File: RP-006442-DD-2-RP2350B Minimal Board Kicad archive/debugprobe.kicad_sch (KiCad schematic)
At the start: 42 parts, among them J4 Conn_01x03, J5 USB_C_Receptacle_USB2.0_16P, SW3 SW_Push, SW4 SW_Push, U5 W25Q128JVS, U6 NCP1117-3.3_SOT223, U7 RP2350_60QFN, Y2 ABM8-272-T3

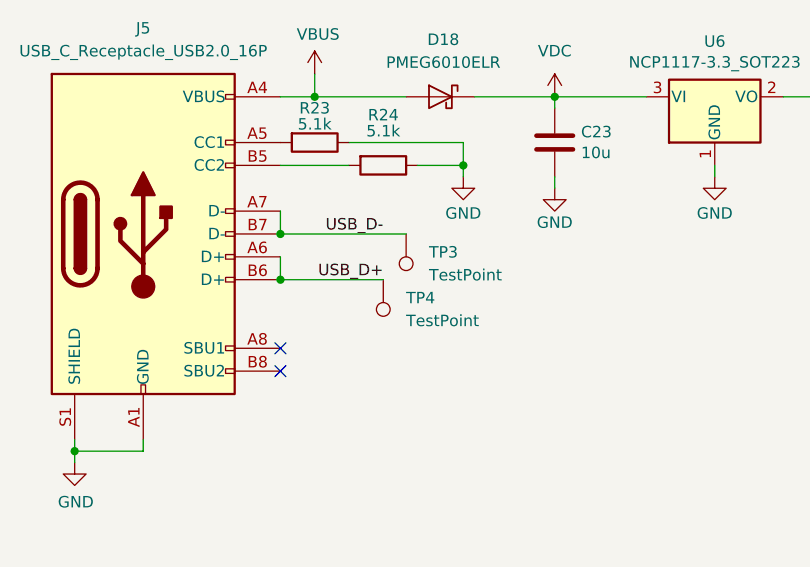
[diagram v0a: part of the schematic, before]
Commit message: Update to schematic and pcb
Changed:
- Added 100n decoupling capacitors to both 74HC595
- Changed ground plane to single common ground plane
- Added schottky diode to usb vbus inputs, creating separate vbus and vsys
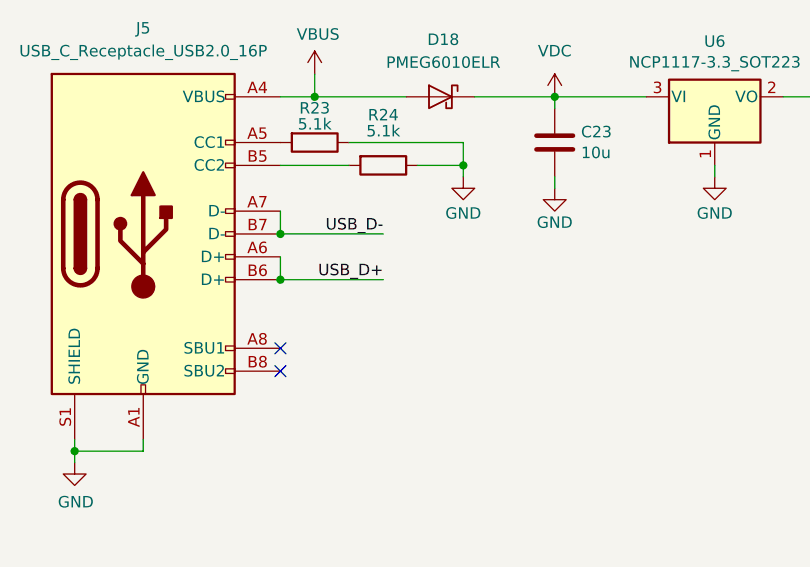
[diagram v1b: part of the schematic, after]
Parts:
- removed TP3, TP4: TestPoint, TestPoint:TestPoint_Pad_2.0x2.0mm, symbol Connector:TestPoint
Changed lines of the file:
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@@
 	)
 	(junction
+		(at 52.07 55.88)
+		(diameter 0)
+		(color 0 0 0 0)
+	)
+	(junction
 		(at 241.3 63.5)
 		(diameter 0)
@@
 	)
 	(junction
-		(at 52.07 55.88)
-		(diameter 0)
-		(color 0 0 0 0)
-	)
-	(junction
 		(at 161.29 73.66)
 		(diameter 0)
@@
 	(wire
 		(pts
-			(xy 298.45 64.77) (xy 298.45 63.5)
+			(xy 52.07 55.88) (xy 63.5 55.88)
 		)
 		(stroke
@@
 	(wire
 		(pts
-			(xy 125.73 118.11) (xy 172.72 118.11)
+			(xy 298.45 64.77) (xy 298.45 63.5)
 		)
 		(stroke
@@
 	(wire
 		(pts
-			(xy 220.98 63.5) (xy 220.98 83.82)
+			(xy 125.73 118.11) (xy 172.72 118.11)
 		)
 		(stroke
@@
 	(wire
 		(pts
-			(xy 252.73 74.93) (xy 241.3 74.93)
+			(xy 220.98 63.5) (xy 220.98 83.82)
 		)
 		(stroke
@@
 	(wire
 		(pts
-			(xy 294.64 189.23) (xy 309.88 189.23)
+			(xy 252.73 74.93) (xy 241.3 74.93)
 		)
 		(stroke
@@
 	(wire
 		(pts
-			(xy 66.04 55.88) (xy 52.07 55.88)
+			(xy 294.64 189.23) (xy 309.88 189.23)
 		)
 		(stroke
@@
 	)
 	(symbol
-		(lib_id "Connector:TestPoint")
-		(at 63.5 60.96 180)
-		(unit 1)
-		(exclude_from_sim no)
-		(in_bom yes)
-		(on_board yes)
-		(dnp no)
-		(fields_autoplaced yes)
-		(property "Reference" "TP4"
-			(at 66.04 62.9919 0)
-			(effects
-				(font
-					(size 1.27 1.27)
-				)
-				(justify right)
-			)
-		)
-		(property "Value" "TestPoint"
-			(at 66.04 65.5319 0)
-			(effects
-				(font
-					(size 1.27 1.27)
-				)
-				(justify right)
-			)
-		)
-		(property "Footprint" "TestPoint:TestPoint_Pad_2.0x2.0mm"
-			(at 58.42 60.96 0)
-			(effects
-				(font
-					(size 1.27 1.27)
-				)
-				(hide yes)
-			)
-		)
-		(property "Datasheet" "~"
-			(at 58.42 60.96 0)
-			(effects
-				(font
-					(size 1.27 1.27)
-				)
-				(hide yes)
-			)
-		)
-		(property "Description" "test point"
-			(at 63.5 60.96 0)
-			(effects
-				(font
-					(size 1.27 1.27)
-				)
-				(hide yes)
-			)
-		)
-		(pin "1"
-		)
-		(instances
-			(project "RP2350_80QFN_minimal"
-				(path "/94683f5c-9cd9-448e-be96-9792537b5cb8/500e1af8-c8c5-44c6-9fbe-f4d5e5ab4ca8"
-					(reference "TP4")
-					(unit 1)
-				)
-			)
-		)
-	)
-	(symbol
 		(lib_id "power:GND")
 		(at 298.45 76.835 0)
@@
 					(unit 1)
 				)
-			)
-		)
-	)
-	(symbol
-		(lib_id "Connector:TestPoint")
-		(at 66.04 55.88 180)
-		(unit 1)
-		(exclude_from_sim no)
-		(in_bom yes)
-		(on_board yes)
-		(dnp no)
-		(fields_autoplaced yes)
-		(property "Reference" "TP3"
-			(at 68.58 57.9119 0)
-			(effects
-				(font
-					(size 1.27 1.27)
-				)
-				(justify right)
-			)
-		)
-		(property "Value" "TestPoint"
-			(at 68.58 60.4519 0)
-			(effects
-				(font
-					(size 1.27 1.27)
-				)
-				(justify right)
-			)
-		)
-		(property "Footprint" "TestPoint:TestPoint_Pad_2.0x2.0mm"
-			(at 60.96 55.88 0)
-			(effects
-				(font
-					(size 1.27 1.27)
-				)
-				(hide yes)
-			)
-		)
-		(property "Datasheet" "~"
-			(at 60.96 55.88 0)
-			(effects
-				(font
-					(size 1.27 1.27)
-				)
-				(hide yes)
-			)
-		)
-		(property "Description" "test point"
-			(at 66.04 55.88 0)
-			(effects
-				(font
-					(size 1.27 1.27)
-				)
-				(hide yes)
-			)
-		)
-		(pin "1"
-		)
-		(instances
-			(project "RP2350_80QFN_minimal"
-				(path "/94683f5c-9cd9-448e-be96-9792537b5cb8/500e1af8-c8c5-44c6-9fbe-f4d5e5ab4ca8"
-					(reference "TP3")
-					(unit 1)
-				)

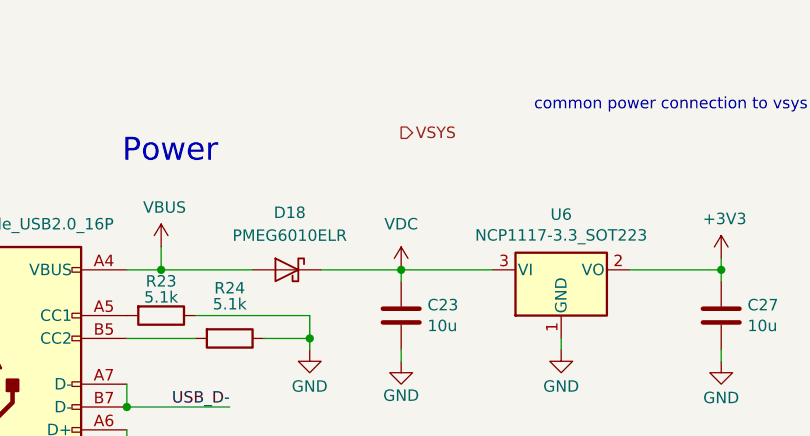
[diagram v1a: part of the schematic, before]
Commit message: Update PCB
Created footprint for SW_SPDT symbol

Added switch footprint to PCB and connected VSYS
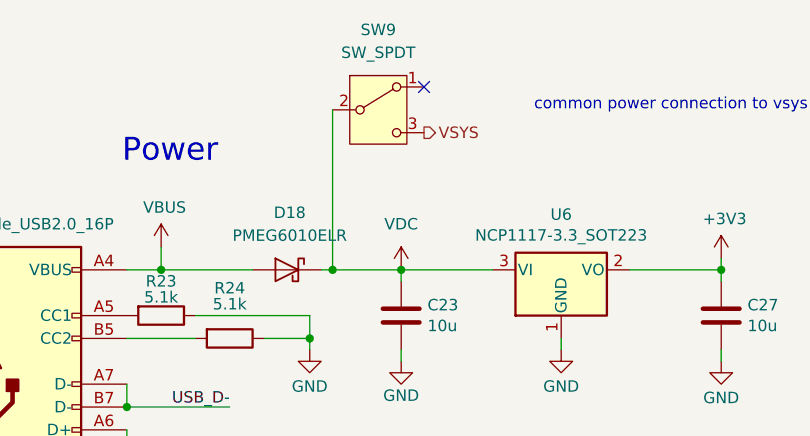
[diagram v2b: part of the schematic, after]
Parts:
- added SW9: SW_SPDT, Button_Switch_SMD:SW_SPDT_HRO_K3-1235S-K1, symbol Switch:SW_SPDT
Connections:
- net VDC: now also SW9.2 (B)
- net VSYS: now also SW9.3 (C)
- no-connect marks 2 -> 3
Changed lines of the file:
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@@
 	)
 	(junction
+		(at 74.93 40.64)
+		(diameter 0)
+		(color 0 0 0 0)
+	)
+	(junction
 		(at 213.36 83.82)
 		(diameter 0)
@@
 	)
 	(no_connect
+		(at 85.09 20.32)
+	)
+	(no_connect
 		(at 52.07 68.58)
 	)
@@
 	(wire
 		(pts
-			(xy 73.66 40.64) (xy 82.55 40.64)
+			(xy 73.66 40.64) (xy 74.93 40.64)
 		)
 		(stroke
@@
 	(wire
 		(pts
+			(xy 74.93 40.64) (xy 82.55 40.64)
+		)
+		(stroke
+			(width 0)
+			(type default)
+		)
+	)
+	(wire
+		(pts
 			(xy 275.59 64.77) (xy 275.59 63.5)
 		)
@@
 	(wire
 		(pts
+			(xy 74.93 22.86) (xy 74.93 40.64)
+		)
+		(stroke
+			(width 0)
+			(type default)
+		)
+	)
+	(wire
+		(pts
 			(xy 90.17 246.38) (xy 91.44 246.38)
 		)
@@
 	(hierarchical_label "VSYS"
 		(shape output)
-		(at 82.55 25.4 0)
+		(at 85.09 25.4 0)
 		(effects
 			(font
@@
 					(unit 1)
 				)
+			)
+		)
+	)
+	(symbol
+		(lib_id "Switch:SW_SPDT")
+		(at 80.01 22.86 0)
+		(unit 1)
+		(exclude_from_sim no)
+		(in_bom yes)
+		(on_board yes)
+		(dnp no)
+		(fields_autoplaced yes)
+		(property "Reference" "SW9"
+			(at 80.01 13.97 0)
+			(effects
+				(font
+					(size 1.27 1.27)
+				)
+			)
+		)
+		(property "Value" "SW_SPDT"
+			(at 80.01 16.51 0)
+			(effects
+				(font
+					(size 1.27 1.27)
+				)
+			)
+		)
+		(property "Footprint" "Button_Switch_SMD:SW_SPDT_HRO_K3-1235S-K1"
+			(at 80.01 22.86 0)
+			(effects
+				(font
+					(size 1.27 1.27)
+				)
+				(hide yes)
+			)
+		)
+		(property "Datasheet" "~"
+			(at 80.01 30.48 0)
+			(effects
+				(font
+					(size 1.27 1.27)
+				)
+				(hide yes)
+			)
+		)
+		(property "Description" "Switch, single pole double throw"
+			(at 80.01 22.86 0)
+			(effects
+				(font
+					(size 1.27 1.27)
+				)
+				(hide yes)
+			)
+		)
+		(pin "1"
+		)
+		(pin "3"
+		)
+		(pin "2"
+		)
+		(instances
+			(project ""
+				(path "/94683f5c-9cd9-448e-be96-9792537b5cb8/500e1af8-c8c5-44c6-9fbe-f4d5e5ab4ca8"
+					(reference "SW9")
+					(unit 1)
+				)

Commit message: Update debugprobe.kicad_sch
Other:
- note removed: "IOs"
- moved on the sheet: C23, C27, C28, C29, C30, C31, C32, C33, C34, C35, C36, C37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

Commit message: Big update
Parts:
- removed D18: PMEG6010ELR, Diode_SMD:Nexperia_CFP3_SOD-123W, symbol Diode:PMEG6010ELR
- added D28: PMEG6010ELR, Diode_SMD:Nexperia_CFP3_SOD-123W, symbol Diode:PMEG6010ELR
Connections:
- net VBUS: now also D28.2 (A)
- net VDC: now also D28.1 (K)
- net GPIO10: no longer names the net of U7.14 (GPIO10)
- net GPIO11: no longer names the net of U7.15 (GPIO11)
- net GPIO12: no longer names the net of U7.16 (GPIO12)
- net GPIO13: no longer names the net of U7.17 (GPIO13)
- net GPIO14: no longer names the net of U7.18 (GPIO14)
- net GPIO15: no longer names the net of U7.19 (GPIO15)
- net GPIO16: no longer names the net of U7.27 (GPIO16)
- net GPIO17: no longer names the net of U7.28 (GPIO17)
- net GPIO18: no longer names the net of U7.29 (GPIO18)
- net GPIO19: no longer names the net of U7.31 (GPIO19)
- net GPIO20: no longer names the net of U7.32 (GPIO20)
- net GPIO21: no longer names the net of U7.33 (GPIO21)
- net GPIO22: no longer names the net of U7.34 (GPIO22)
- net GPIO23: no longer names the net of U7.35 (GPIO23)
- net GPIO24: no longer names the net of U7.36 (GPIO24)
- net GPIO25: no longer names the net of U7.37 (GPIO25)
- net GPIO26_ADC0: no longer names the net of U7.40 (GPIO26_ADC0)
- net GPIO27_ADC1: no longer names the net of U7.41 (GPIO27_ADC1)
- net GPIO28_ADC2: no longer names the net of U7.42 (GPIO28_ADC2)
- net GPIO29_ADC3: no longer names the net of U7.43 (GPIO29_ADC3)
- net GPIO6: no longer names the net of U7.9 (GPIO6)
- net GPIO7: no longer names the net of U7.10 (GPIO7)
- net GPIO8: no longer names the net of U7.12 (GPIO8)
- net GPIO9: no longer names the net of U7.13 (GPIO9)
- no-connect marks 3 -> 28

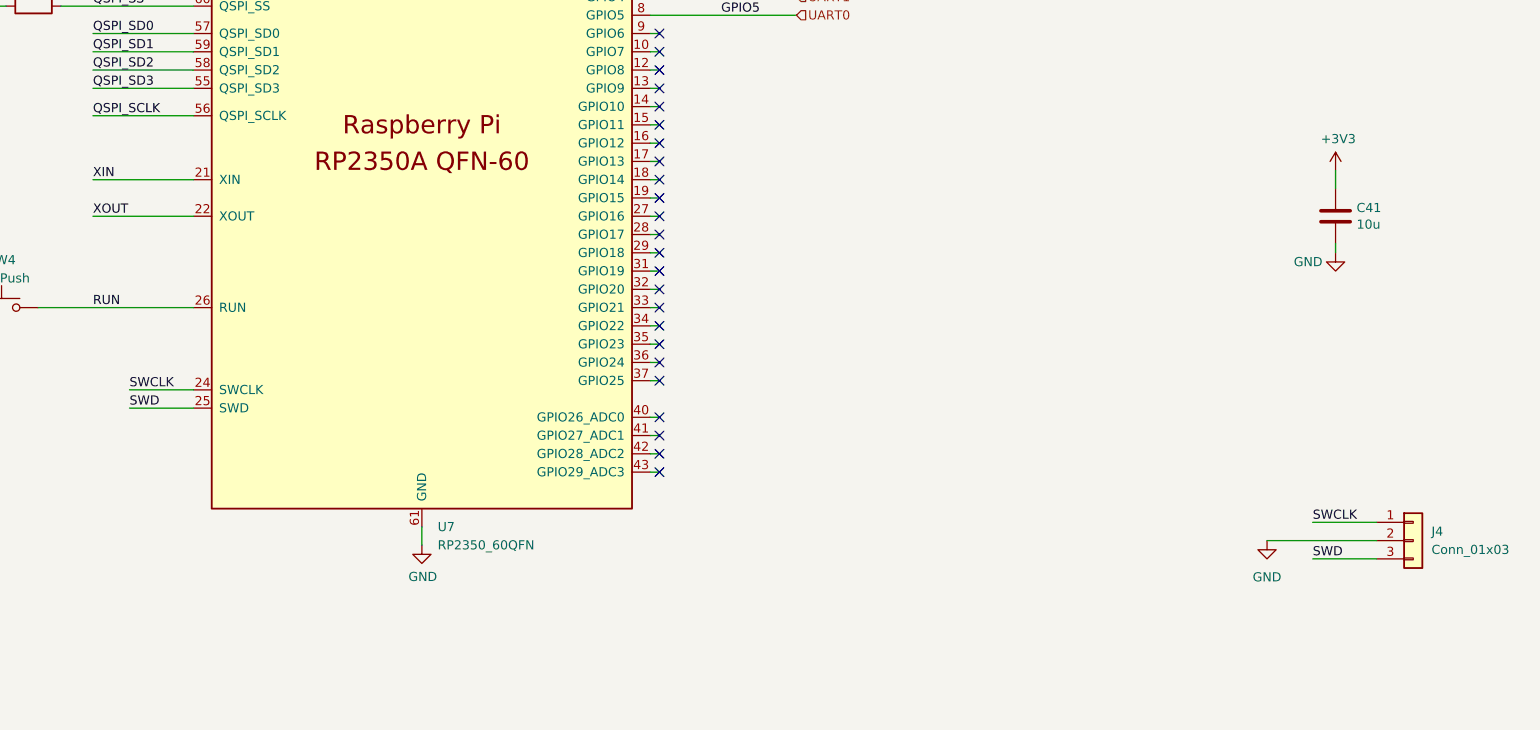
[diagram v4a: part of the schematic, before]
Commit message: Changed edgecuts to within 100mmX100mm
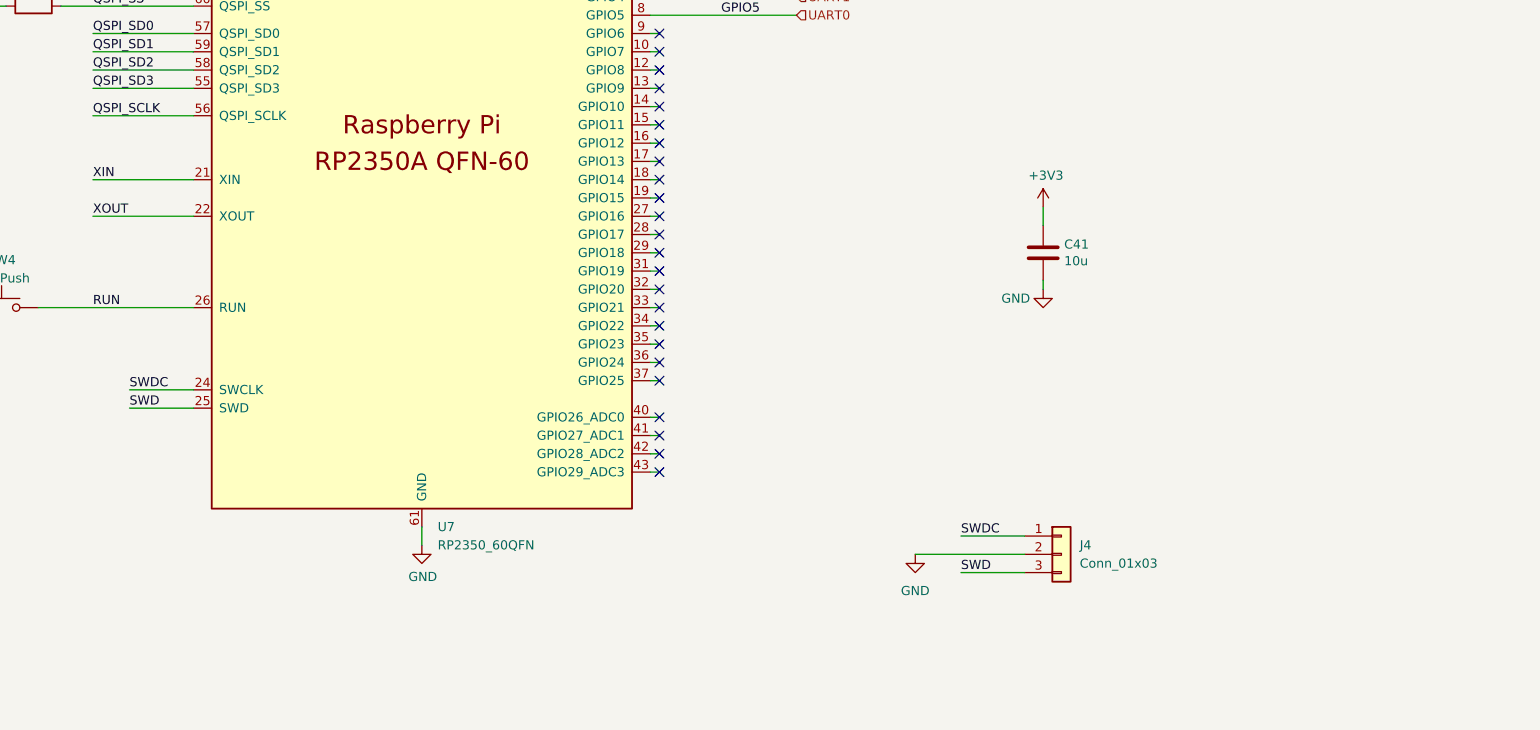
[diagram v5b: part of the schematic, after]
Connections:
- net SWCLK: no longer J4.1 (Pin_1), U7.24 (SWCLK)
- new net SWDC: J4.1 (Pin_1), U7.24 (SWCLK)
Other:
- moved on the sheet: C41, J4
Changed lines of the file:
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@@
 	(wire
 		(pts
-			(xy 359.41 175.26) (xy 359.41 176.53)
+			(xy 318.77 180.34) (xy 318.77 181.61)
 		)
 		(stroke
@@
 	(wire
 		(pts
-			(xy 349.885 216.535) (xy 365.125 216.535)
+			(xy 300.99 218.44) (xy 316.23 218.44)
 		)
 		(stroke
@@
 	(wire
 		(pts
-			(xy 356.235 213.995) (xy 365.125 213.995)
-		)
-		(stroke
-			(width 0)
-			(type default)
-		)
-	)
-	(wire
-		(pts
 			(xy 209.55 78.74) (xy 209.55 80.01)
 		)
@@
 	(wire
 		(pts
-			(xy 359.41 165.1) (xy 359.41 167.64)
+			(xy 318.77 170.18) (xy 318.77 172.72)
 		)
 		(stroke
@@
 	(wire
 		(pts
-			(xy 356.235 219.075) (xy 365.125 219.075)
+			(xy 307.34 220.98) (xy 316.23 220.98)
 		)
 		(stroke
@@
 	(wire
 		(pts
+			(xy 307.34 215.9) (xy 316.23 215.9)
+		)
+		(stroke
+			(width 0)
+			(type default)
+		)
+	)
+	(wire
+		(pts
 			(xy 88.9 40.64) (xy 88.9 58.42)
 		)
@@
 		)
 	)
-	(label "SWCLK"
-		(at 356.235 213.995 0)
+	(label "VREG_AVDD"
+		(at 188.595 109.22 0)
 		(effects
 			(font
@@
 		)
 	)
-	(label "VREG_AVDD"
-		(at 188.595 109.22 0)
+	(label "QSPI_SD3"
+		(at 186.69 153.67 0)
 		(effects
 			(font
@@
 		)
 	)
-	(label "QSPI_SD3"
-		(at 186.69 153.67 0)
+	(label "SWDC"
+		(at 307.34 215.9 0)
 		(effects
 			(font
@@
 	)
 	(label "SWD"
-		(at 356.235 219.075 0)
+		(at 307.34 220.98 0)
 		(effects
 			(font
@@
 		)
 	)
-	(label "SWCLK"
-		(at 191.77 195.58 0)
-		(effects
-			(font
-				(size 1.27 1.27)
-			)
-			(justify left bottom)
-		)
-	)
 	(label "XOUT"
 		(at 186.69 171.45 0)
@@
 		)
 	)
+	(label "SWDC"
+		(at 191.77 195.58 0)
+		(effects
+			(font
+				(size 1.27 1.27)
+			)
+			(justify left bottom)
+		)
+	)
 	(label "QSPI_SD0"
 		(at 186.69 146.05 0)
@@
 	(symbol
 		(lib_id "power:+3V3")
-		(at 359.41 165.1 0)
+		(at 318.77 170.18 0)
 		(unit 1)
 		(exclude_from_sim no)
@@
 		(dnp no)
 		(property "Reference" "#PWR057"
-			(at 359.41 168.91 0)
+			(at 318.77 173.99 0)
 			(effects
 				(font
@@
 		)
 		(property "Value" "+3V3"
-			(at 359.791 160.7058 0)
+			(at 319.151 165.7858 0)
 			(effects
 				(font
@@
 		)
 		(property "Footprint" ""
-			(at 359.41 165.1 0)
+			(at 318.77 170.18 0)
 			(effects
 				(font
@@
 		)
 		(property "Datasheet" ""
-			(at 359.41 165.1 0)
+			(at 318.77 170.18 0)
 			(effects
 				(font
@@
 		)
 		(property "Description" ""
-			(at 359.41 165.1 0)
+			(at 318.77 170.18 0)
 			(effects
 				(font
@@
 	(symbol
 		(lib_id "Connector_Generic:Conn_01x03")
-		(at 370.205 216.535 0)
+		(at 321.31 218.44 0)
 		(unit 1)
 		(exclude_from_sim no)
@@
 		(fields_autoplaced yes)
 		(property "Reference" "J4"
-			(at 372.745 215.2649 0)
+			(at 323.85 217.1699 0)
 			(effects
 				(font
@@
 		)
 		(property "Value" "Conn_01x03"
-			(at 372.745 217.8049 0)
+			(at 323.85 219.7099 0)
 			(effects
 				(font
@@
 		)
 		(property "Footprint" "Connector_PinHeader_2.54mm:PinHeader_1x03_P2.54mm_Vertical"
-			(at 370.205 216.535 0)
+			(at 321.31 218.44 0)
 			(effects
 				(font
@@
 		)
 		(property "Datasheet" "~"
-			(at 370.205 216.535 0)
+			(at 321.31 218.44 0)
 			(effects
 				(font
@@
 		)
 		(property "Description" "Generic connector, single row, 01x03, script generated (kicad-library-utils/schlib/autogen/connector/)"
-			(at 370.205 216.535 0)
+			(at 321.31 218.44 0)
 			(effects
 				(font
@@
 	(symbol
 		(lib_id "Device:C")
-		(at 359.41 171.45 0)
+		(at 318.77 176.53 0)
 		(unit 1)
 		(exclude_from_sim no)
@@
 		(dnp no)
 		(property "Reference" "C41"
-			(at 362.331 170.2816 0)
+			(at 321.691 175.3616 0)
 			(effects
 				(font
@@
 		)
 		(property "Value" "10u"
-			(at 362.331 172.593 0)
+			(at 321.691 177.673 0)
 			(effects
 				(font
@@
 		)
 		(property "Footprint" "Capacitor_SMD:C_0805_2012Metric"
-			(at 360.3752 175.26 0)
+			(at 319.7352 180.34 0)
 			(effects
 				(font
@@
 		)
 		(property "Datasheet" "~"
-			(at 359.41 171.45 0)
+			(at 318.77 176.53 0)
 			(effects
 				(font
@@
 		)
 		(property "Description" ""
-			(at 359.41 171.45 0)
+			(at 318.77 176.53 0)
 			(effects
 				(font
@@
 		(lib_name "GND_1")
 		(lib_id "power:GND")
-		(at 349.885 216.535 0)
+		(at 300.99 218.44 0)
 		(unit 1)
 		(exclude_from_sim no)
@@
 		(fields_autoplaced yes)
 		(property "Reference" "#PWR067"
-			(at 349.885 222.885 0)
+			(at 300.99 224.79 0)
 			(effects
 				(font
@@
 		)
 		(property "Value" "GND"
-			(at 349.885 221.615 0)
+			(at 300.99 223.52 0)
 			(effects
 				(font
@@
 		)
 		(property "Footprint" ""
-			(at 349.885 216.535 0)
+			(at 300.99 218.44 0)
 			(effects
 				(font
@@
 		)
 		(property "Datasheet" ""
-			(at 349.885 216.535 0)
+			(at 300.99 218.44 0)
 			(effects
 				(font
@@
 		)
 		(property "Description" "Power symbol creates a global label with name \"GND\" , ground"
-			(at 349.885 216.535 0)
+			(at 300.99 218.44 0)
 			(effects
 				(font
@@
 	(symbol
 		(lib_id "power:GND")
-		(at 359.41 176.53 0)
+		(at 318.77 181.61 0)
 		(unit 1)
 		(exclude_from_sim no)
@@
 		(dnp no)
 		(property "Reference" "#PWR058"
-			(at 359.41 182.88 0)
+			(at 318.77 187.96 0)
 			(effects
 				(font
@@
 		)
 		(property "Value" "GND"
-			(at 355.6 177.8 0)
+			(at 314.96 182.88 0)
 			(effects
 				(font
@@
 		)
 		(property "Footprint" ""
-			(at 359.41 176.53 0)
+			(at 318.77 181.61 0)
 			(effects
 				(font
@@
 		)
 		(property "Datasheet" ""
-			(at 359.41 176.53 0)
+			(at 318.77 181.61 0)
 			(effects
 				(font
@@
 		)
 		(property "Description" ""
-			(at 359.41 176.53 0)
+			(at 318.77 181.61 0)
 			(effects
 				(font
